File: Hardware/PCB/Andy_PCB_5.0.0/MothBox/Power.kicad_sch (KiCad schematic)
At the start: 27 parts, among them P1 Raw Input, P2 12V Regulated Input, P3 Input to regulator, Q1 BC817, Q2 TJ10S04M3L,LXHQ, U15 Place Holder voltage regulator, U19 INA219BIDCNT, U3 XL4015E1

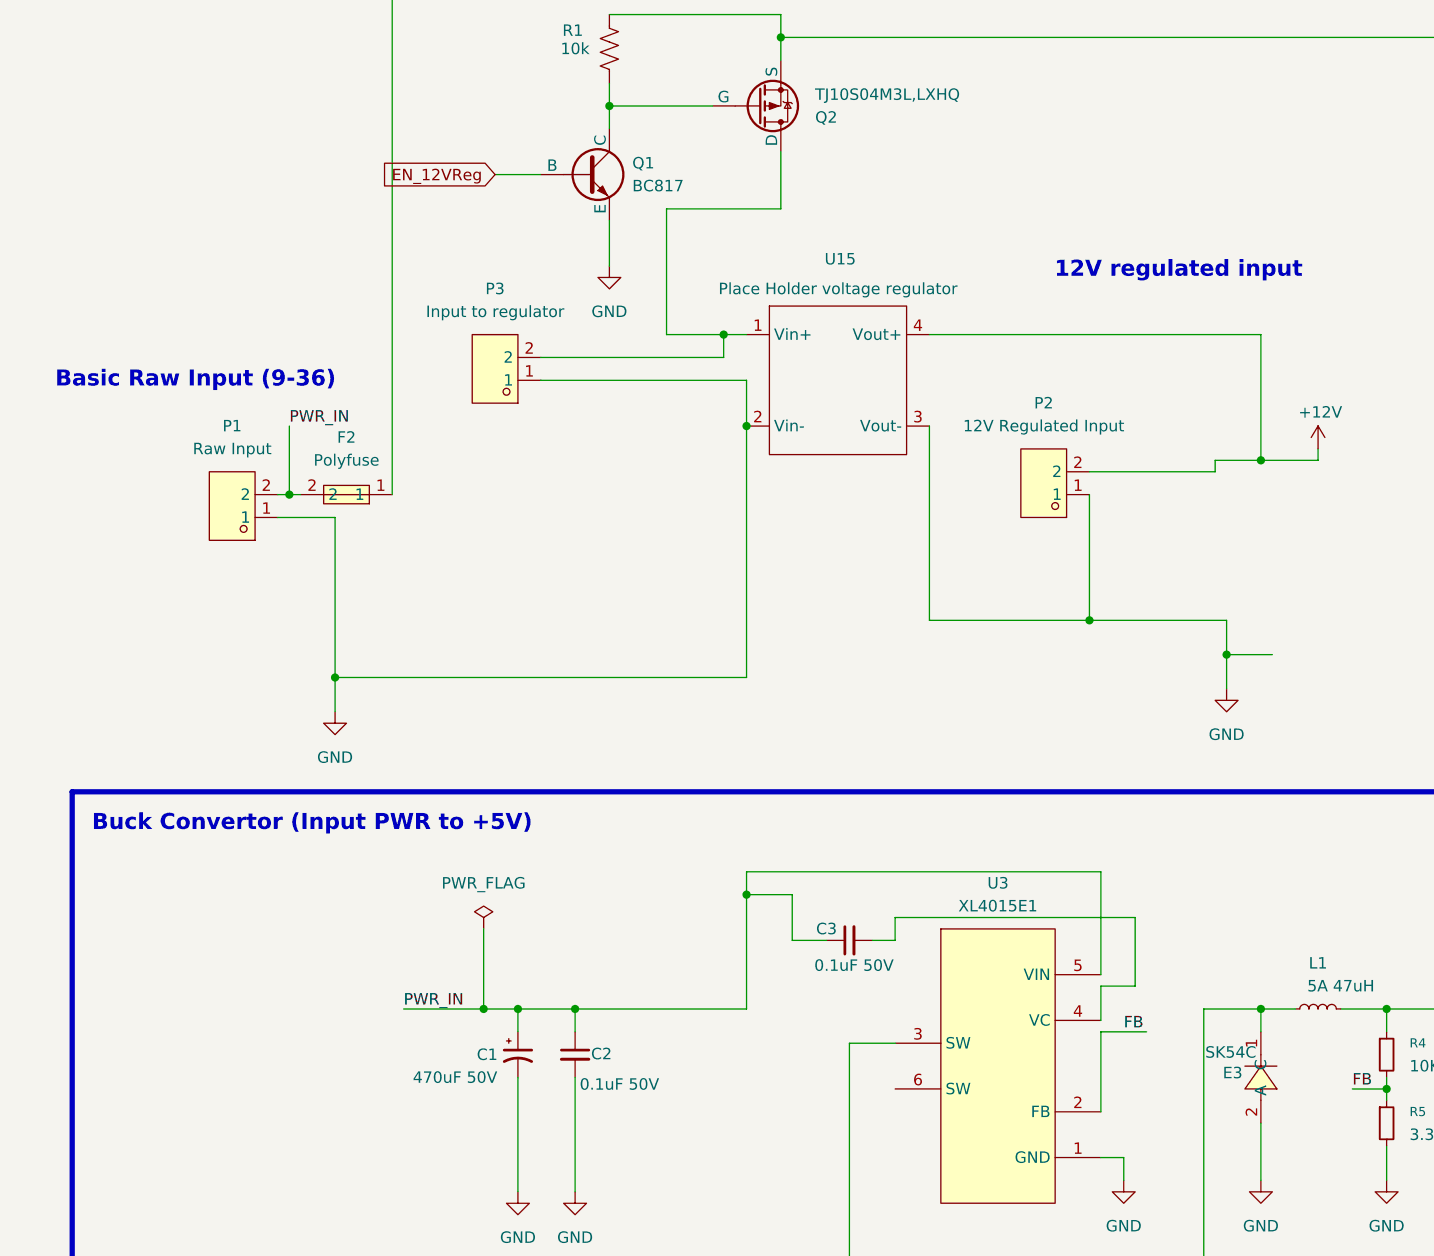
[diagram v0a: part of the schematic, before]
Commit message: cleaned most schematic and got rid of half errors in ERC
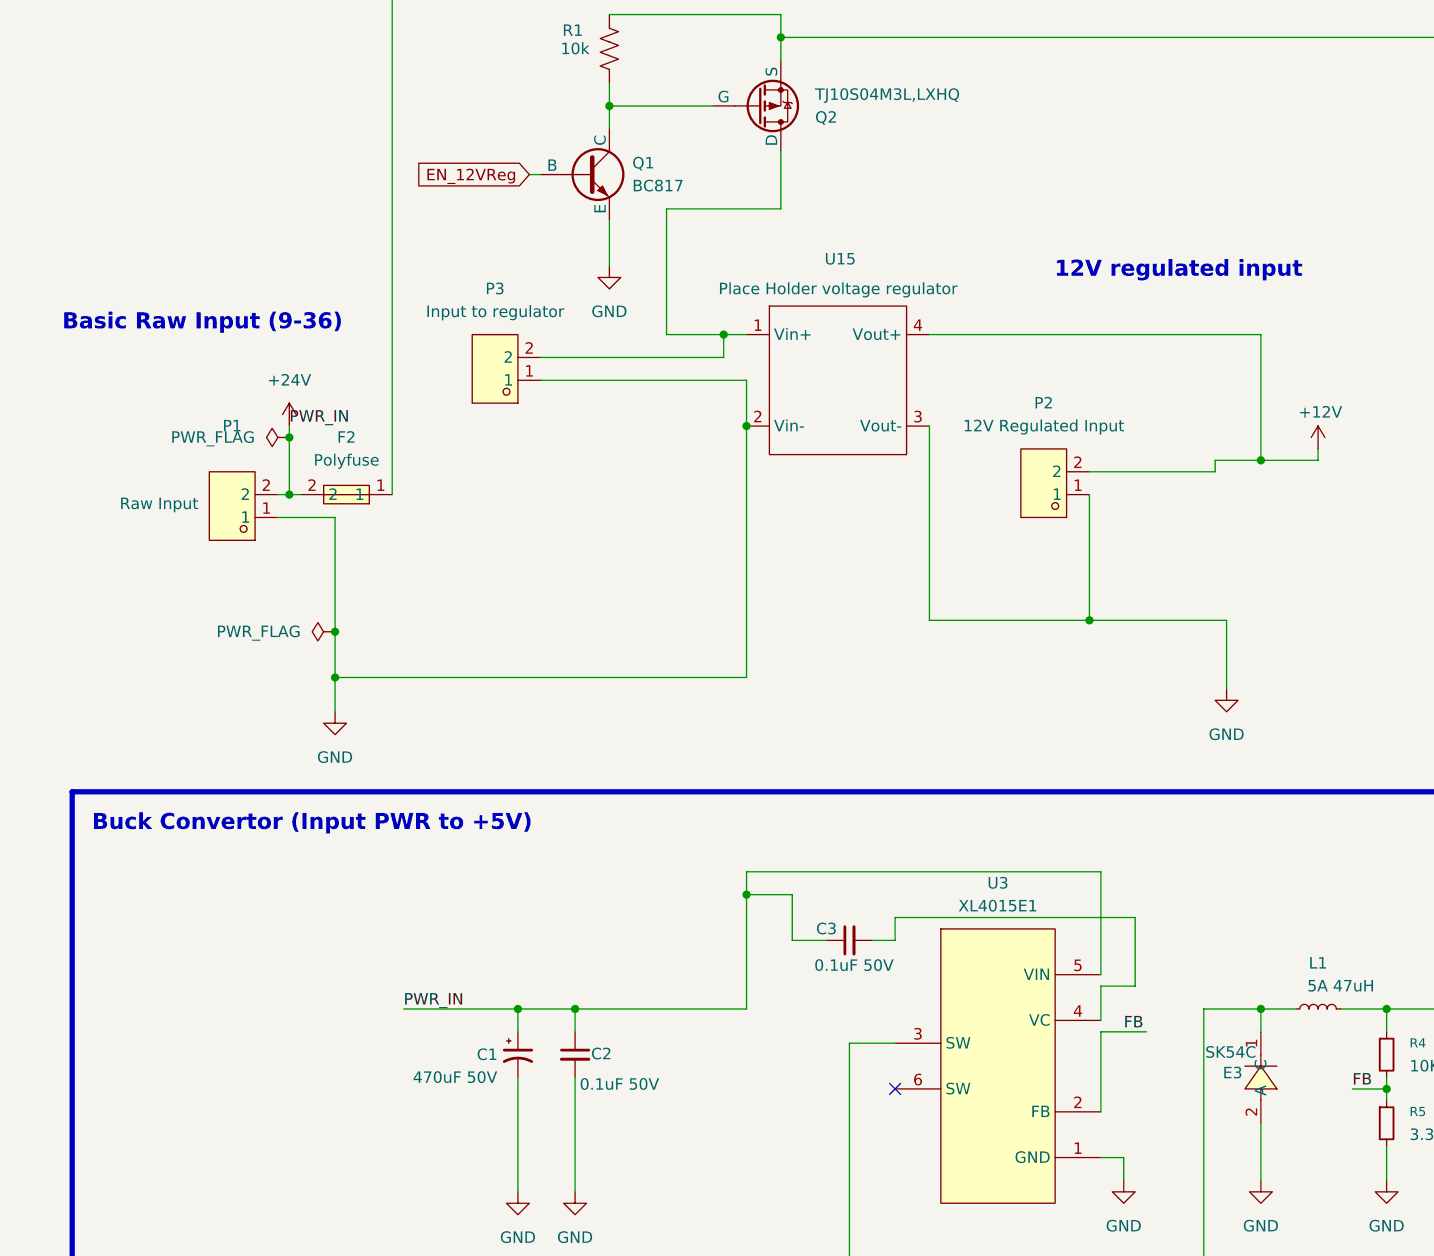
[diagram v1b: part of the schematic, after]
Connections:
- net PWR_IN renamed +24V
- no-connect marks 0 -> 1

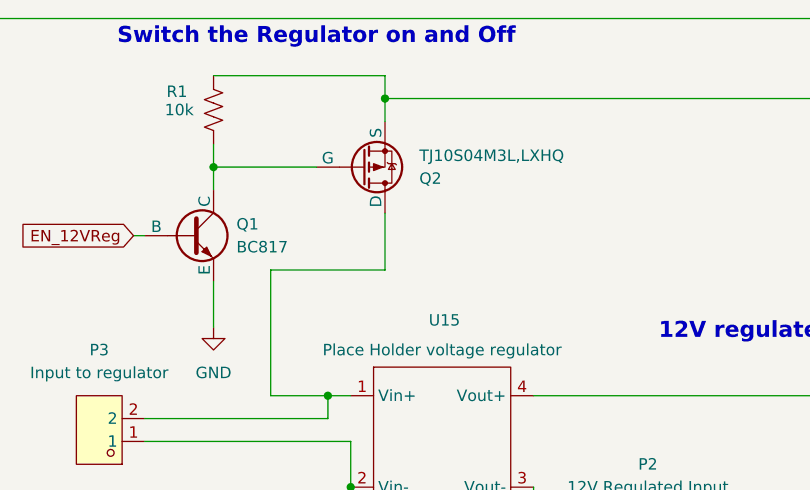
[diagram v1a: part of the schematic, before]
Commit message: Fixed parts with conflicting LCSC footprints
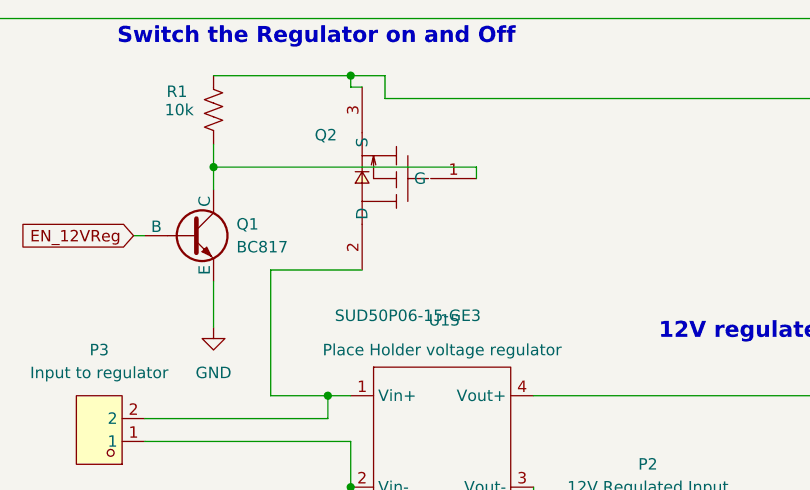
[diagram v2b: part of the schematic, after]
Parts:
- Q2: value TJ10S04M3L,LXHQ -> SUD50P06-15-GE3; footprint Package_TO_SOT_SMD:TO-252-2 -> easyeda2kicad:TO-252-3_L6.5-W5.8-P4.58-BL; symbol Simulation_SPICE:PMOS -> easyeda2kicad:SUD50P06-15-GE3; Digikey Part No TJ10S04M3L,LXHQ -> (none); LCSC Part (none) -> C141584; LCSC Part no  C41355200 -> (none)
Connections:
- net at Q1.3 (C), R1.1: now also Q2.1 (G); no longer Q2.2 (G)
- net at P3.2, U15.1 (Vin+): now also Q2.2 (D); no longer Q2.1 (D)
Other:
- moved on the sheet: Q2
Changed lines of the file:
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@@
 	)
 	(junction
-		(at 106.68 22.86)
+		(at 102.87 20.32)
 		(diameter 0)
 		(color 0 0 0 0)
@@
 	(wire
 		(pts
+			(xy 102.87 20.32) (xy 106.68 20.32)
+		)
+		(stroke
+			(width 0)
+			(type default)
+		)
+	)
+	(wire
+		(pts
 			(xy 267.97 49.53) (xy 267.97 44.45)
 		)
@@
 	(wire
 		(pts
-			(xy 106.68 41.91) (xy 106.68 35.56)
-		)
-		(stroke
-			(width 0)
-			(type default)
-		)
-	)
-	(wire
-		(pts
 			(xy 254 55.88) (xy 257.81 55.88)
 		)
@@
 	(wire
 		(pts
-			(xy 106.68 22.86) (xy 106.68 25.4)
-		)
-		(stroke
-			(width 0)
-			(type default)
-		)
-	)
-	(wire
-		(pts
 			(xy 102.87 118.11) (xy 102.87 130.81)
 		)
@@
 	(wire
 		(pts
-			(xy 93.98 41.91) (xy 106.68 41.91)
+			(xy 93.98 41.91) (xy 104.14 41.91)
 		)
 		(stroke
@@
 	(wire
 		(pts
+			(xy 102.87 21.59) (xy 102.87 20.32)
+		)
+		(stroke
+			(width 0)
+			(type default)
+		)
+	)
+	(wire
+		(pts
 			(xy 100.33 58.42) (xy 100.33 55.88)
 		)
@@
 	(wire
 		(pts
-			(xy 87.63 20.32) (xy 106.68 20.32)
+			(xy 87.63 20.32) (xy 102.87 20.32)
 		)
 		(stroke
@@
 	(wire
 		(pts
+			(xy 104.14 21.59) (xy 102.87 21.59)
+		)
+		(stroke
+			(width 0)
+			(type default)
+		)
+	)
+	(wire
+		(pts
 			(xy 318.77 54.61) (xy 303.53 54.61)
 		)
@@
 	(wire
 		(pts
-			(xy 87.63 30.48) (xy 99.06 30.48)
+			(xy 87.63 30.48) (xy 116.84 30.48)
 		)
 		(stroke
@@
 	(wire
 		(pts
+			(xy 116.84 30.48) (xy 116.84 31.75)
+		)
+		(stroke
+			(width 0)
+			(type default)
+		)
+	)
+	(wire
+		(pts
 			(xy 160.02 143.51) (xy 160.02 149.86)
 		)
@@
 	)
 	(symbol
-		(lib_id "Simulation_SPICE:PMOS")
-		(at 104.14 30.48 0)
-		(mirror x)
+		(lib_id "easyeda2kicad:SUD50P06-15-GE3")
+		(at 109.22 31.75 0)
+		(mirror y)
 		(unit 1)
 		(exclude_from_sim no)
@@
 		(on_board yes)
 		(dnp no)
-		(fields_autoplaced yes)
 		(property "Reference" "Q2"
-			(at 110.49 31.7501 0)
-			(effects
-				(font
-					(size 1.27 1.27)
-				)
-				(justify left)
-			)
-		)
-		(property "Value" "TJ10S04M3L,LXHQ"
-			(at 110.49 29.2101 0)
+			(at 101.346 26.924 0)
 			(effects
 				(font
@@
 			)
 		)
-		(property "Footprint" "Package_TO_SOT_SMD:TO-252-2"
-			(at 109.22 33.02 0)
+		(property "Value" "SUD50P06-15-GE3"
+			(at 109.22 46.99 0)
 			(effects
 				(font
 					(size 1.27 1.27)
 				)
-				(hide yes)
 			)
 		)
-		(property "Datasheet" "https://ngspice.sourceforge.io/docs/ngspice-html-manual/manual.xhtml#cha_MOSFETs"
-			(at 104.14 17.78 0)
+		(property "Footprint" "easyeda2kicad:TO-252-3_L6.5-W5.8-P4.58-BL"
+			(at 109.22 49.53 0)
 			(effects
 				(font
@@
 			)
 		)
-		(property "Description" "P-Channel 40 V 10A (Ta) 27W (Tc) Surface Mount DPAK+"
-			(at 104.14 30.48 0)
+		(property "Datasheet" "https://lcsc.com/product-detail/MOSFET_VISHAY_SUD50P06-15-GE3_SUD50P06-15-GE3_C141584.html"
+			(at 109.22 52.07 0)
 			(effects
 				(font
@@
 			)
 		)
-		(property "Sim.Device" "PMOS"
-			(at 104.14 13.335 0)
-			(effects
-				(font
-					(size 1.27 1.27)
-				)
-				(hide yes)
-			)
-		)
-		(property "Sim.Type" "VDMOS"
-			(at 104.14 11.43 0)
-			(effects
-				(font
-					(size 1.27 1.27)
-				)
-				(hide yes)
-			)
-		)
-		(property "Sim.Pins" "1=D 2=G 3=S"
-			(at 104.14 15.24 0)
-			(effects
-				(font
-					(size 1.27 1.27)
-				)
-				(hide yes)
-			)
-		)
-		(property "LCSC Part no " "C41355200"
-			(at 104.14 30.48 0)
+		(property "Description" ""
+			(at 109.22 31.75 0)
 			(effects
 				(font
@@
 			)
 		)
-		(property "Digikey Part No" "TJ10S04M3L,LXHQ"
-			(at 104.14 30.48 0)
+		(property "LCSC Part" "C141584"
+			(at 109.22 54.61 0)
 			(effects
 				(font
@@
 			)
 		)
-		(property "LCSC PN" ""
-			(at 104.14 30.48 0)
-			(effects
-				(font
-					(size 1.27 1.27)
-				)
-			)
-		)

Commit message: Maybe these files needed saving too for paul?
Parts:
- C1, C4: symbol Device:C_Polarized_Small_US -> MB_Library:C_Polarized_Small_US
- C2, C3, C5: symbol Device:C_Small -> MB_Library:C_Small
- C6: symbol easyeda2kicad:CC0603KRX7R9BB104 -> MB_Library:CC0603KRX7R9BB104
- E3: symbol easyeda2kicad:SK54C_C5449119 -> MB_Library:SK54C_C5449119
- F2: symbol easyeda2kicad:0805L010_60WR -> MB_Library:0805L010_60WR
- L1: symbol Device:L_Small -> MB_Library:L_Small
- P1, P2, P3: symbol easyeda2kicad:DB142R-5.08-2P -> MB_Library:DB142R-5.08-2P
- Q1: symbol BC817:BC817_NPN_BJT -> MB_Library:BC817_NPN_BJT
- Q2: symbol easyeda2kicad:SUD50P06-15-GE3 -> MB_Library:SUD50P06-15-GE3
- R1: symbol Device:R_US -> MB_Library:R_US
- R4, R5: symbol Device:R_Small -> MB_Library:R_Small
- R63: symbol easyeda2kicad:PCSR2512BR100M6 -> MB_Library:PCSR2512BR100M6
- R64, R65: symbol easyeda2kicad:FRC0603J103TS -> MB_Library:FRC0603J103TS
- TP1, TP2, TP3, TP4: symbol Connector:TestPoint -> MB_Library:TestPoint
- U15: symbol New_Library:Buck-Boost -> MB_Library:Buck-Boost
- U19: symbol easyeda2kicad:INA219AIDCNR -> MB_Library:INA219AIDCNR
- U3: symbol easyeda2kicad:XL4015E1 -> MB_Library:XL4015E1
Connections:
- net GND: no longer C6.1, U19.3 (GND)
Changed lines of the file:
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@@
 	)
 	(symbol
-		(lib_id "power:GND")
+		(lib_id "MB_Library:GND")
 		(at 156.21 95.25 0)
 		(unit 1)
@@
 	)
 	(symbol
-		(lib_id "BC817:BC817_NPN_BJT")
+		(lib_id "MB_Library:BC817_NPN_BJT")
 		(at 85.09 38.1 0)
 		(unit 1)
@@
 	)
 	(symbol
-		(lib_id "easyeda2kicad:PCSR2512BR100M6")
+		(lib_id "MB_Library:PCSR2512BR100M6")
 		(at 273.05 52.07 90)
 		(unit 1)
@@
 	)
 	(symbol
-		(lib_id "easyeda2kicad:DB142R-5.08-2P")
+		(lib_id "MB_Library:DB142R-5.08-2P")
 		(at 135.89 72.39 180)
 		(unit 1)
@@
 	)
 	(symbol
-		(lib_id "easyeda2kicad:DB142R-5.08-2P")
+		(lib_id "MB_Library:DB142R-5.08-2P")
 		(at 74.93 59.69 180)
 		(unit 1)
@@
 	)
 	(symbol
-		(lib_id "easyeda2kicad:SK54C_C5449119")
+		(lib_id "MB_Library:SK54C_C5449119")
 		(at 160.02 138.43 270)
 		(unit 1)
@@
 	)
 	(symbol
-		(lib_id "easyeda2kicad:XL4015E1")
+		(lib_id "MB_Library:XL4015E1")
 		(at 130.81 137.16 0)
 		(unit 1)
@@
 	)
 	(symbol
-		(lib_id "Connector:TestPoint")
+		(lib_id "MB_Library:TestPoint")
 		(at 269.24 62.23 180)
 		(unit 1)
@@
 	)
 	(symbol
-		(lib_id "power:+12V")
+		(lib_id "MB_Library:+12V")
 		(at 166.37 68.58 0)
 		(unit 1)
@@
 	)
 	(symbol
-		(lib_id "power:+24V")
+		(lib_id "MB_Library:+24V")
 		(at 52.07 66.04 0)
 		(unit 1)
@@
 	)
 	(symbol
-		(lib_id "power:PWR_FLAG")
+		(lib_id "MB_Library:PWR_FLAG")
 		(at 52.07 67.31 90)
 		(unit 1)
@@
 	)
 	(symbol
-		(lib_id "easyeda2kicad:CC0603KRX7R9BB104")
+		(lib_id "MB_Library:CC0603KRX7R9BB104")
 		(at 214.63 41.91 90)
 		(unit 1)
@@
 	)
 	(symbol
-		(lib_id "Connector:TestPoint")
+		(lib_id "MB_Library:TestPoint")
 		(at 232.41 57.15 90)
 		(unit 1)
@@
 	)
 	(symbol
-		(lib_id "Connector:TestPoint")
+		(lib_id "MB_Library:TestPoint")
 		(at 223.52 54.61 90)
 		(unit 1)
@@
 	)
 	(symbol
-		(lib_id "power:GND")
+		(lib_id "MB_Library:GND")
 		(at 200.66 149.86 0)
 		(unit 1)
@@
 	)
 	(symbol
-		(lib_id "Device:C_Small")
+		(lib_id "MB_Library:C_Small")
 		(at 200.66 138.43 0)
 		(unit 1)
@@
 	)
 	(symbol
-		(lib_id "Adafruit_INA219_CurPowerMonitor-eagle-import:GND")
+		(lib_id "MB_Library:GND")
 		(at 229.87 74.93 0)
 		(unit 1)
@@
 	)
 	(symbol
-		(lib_id "Device:L_Small")
+		(lib_id "MB_Library:L_Small")
 		(at 166.37 130.81 90)
 		(unit 1)
@@
 	)
 	(symbol
-		(lib_id "power:+3.3V")
+		(lib_id "MB_Library:+3.3V")
 		(at 295.91 31.75 0)
 		(unit 1)
@@
 	)
 	(symbol
-		(lib_id "Device:C_Small")
+		(lib_id "MB_Library:C_Small")
 		(at 114.3 123.19 90)
 		(unit 1)
@@
 	)
 	(symbol
-		(lib_id "power:GND")
+		(lib_id "MB_Library:GND")
 		(at 83.82 151.13 0)
 		(unit 1)
@@
 	)
 	(symbol
-		(lib_id "power:PWR_FLAG")
+		(lib_id "MB_Library:PWR_FLAG")
 		(at 57.15 88.9 90)
 		(unit 1)
@@
 	)
 	(symbol
-		(lib_id "power:GND")
+		(lib_id "MB_Library:GND")
 		(at 187.96 149.86 0)
 		(unit 1)
@@
 	)
 	(symbol
-		(lib_id "Device:R_Small")
+		(lib_id "MB_Library:R_Small")
 		(at 173.99 143.51 0)
 		(unit 1)
@@
 	)
 	(symbol
-		(lib_id "easyeda2kicad:DB142R-5.08-2P")
+		(lib_id "MB_Library:DB142R-5.08-2P")
 		(at 45.72 74.93 180)
 		(unit 1)
@@
 	)
 	(symbol
-		(lib_id "power:GND")
+		(lib_id "MB_Library:GND")
 		(at 77.47 151.13 0)
 		(unit 1)
@@
 	)
 	(symbol
-		(lib_id "power:GND")
+		(lib_id "MB_Library:GND")
 		(at 144.78 149.86 0)
 		(unit 1)
@@
 	)
 	(symbol
-		(lib_id "Connector:TestPoint")
+		(lib_id "MB_Library:TestPoint")
 		(at 190.5 130.81 0)
 		(unit 1)
@@
 	)
 	(symbol
-		(lib_id "Device:R_Small")
+		(lib_id "MB_Library:R_Small")
 		(at 173.99 135.89 0)
 		(unit 1)
@@
 	)
 	(symbol
-		(lib_id "Adafruit_INA219_CurPowerMonitor-eagle-import:GND")
+		(lib_id "MB_Library:GND")
 		(at 207.01 49.53 0)
 		(unit 1)
@@
 	)
 	(symbol
-		(lib_id "easyeda2kicad:FRC0603J103TS")
+		(lib_id "MB_Library:FRC0603J103TS")
 		(at 295.91 39.37 90)
 		(unit 1)
@@
 	)
 	(symbol
-		(lib_id "Device:C_Polarized_Small_US")
+		(lib_id "MB_Library:C_Polarized_Small_US")
 		(at 77.47 135.89 0)
 		(unit 1)
@@
 	)
 	(symbol
-		(lib_id "Device:R_US")
+		(lib_id "MB_Library:R_US")
 		(at 87.63 24.13 180)
 		(unit 1)
@@
 	)
 	(symbol
-		(lib_id "New_Library:Buck-Boost")
+		(lib_id "MB_Library:Buck-Boost")
 		(at 113.03 60.96 0)
 		(unit 1)
@@
 	)
 	(symbol
-		(lib_id "power:GND")
+		(lib_id "MB_Library:GND")
 		(at 173.99 149.86 0)
 		(unit 1)
@@
 	)
 	(symbol
-		(lib_id "power:GND")
+		(lib_id "MB_Library:GND")
 		(at 57.15 97.79 0)
 		(unit 1)
@@
 	)
 	(symbol
-		(lib_id "power:+5V")
+		(lib_id "MB_Library:+5V")
 		(at 200.66 129.54 0)
 		(unit 1)
@@
 	)
 	(symbol
-		(lib_id "power:GND")
+		(lib_id "MB_Library:GND")
 		(at 160.02 149.86 0)
 		(unit 1)
@@
 	)
 	(symbol
-		(lib_id "easyeda2kicad:INA219AIDCNR")
+		(lib_id "MB_Library:INA219AIDCNR")
 		(at 243.84 52.07 180)
 		(unit 1)
@@
 	)
 	(symbol
-		(lib_id "easyeda2kicad:SUD50P06-15-GE3")
+		(lib_id "MB_Library:SUD50P06-15-GE3")
 		(at 109.22 31.75 0)
 		(mirror y)
@@
 	)
 	(symbol
-		(lib_id "power:+3.3V")
+		(lib_id "MB_Library:+3.3V")
 		(at 207.01 31.75 0)
 		(unit 1)
@@
 	)
 	(symbol
-		(lib_id "easyeda2kicad:FRC0603J103TS")
+		(lib_id "MB_Library:FRC0603J103TS")
 		(at 303.53 39.37 90)
 		(unit 1)
@@
 	)
 	(symbol
-		(lib_id "Device:C_Polarized_Small_US")
+		(lib_id "MB_Library:C_Polarized_Small_US")
 		(at 187.96 138.43 0)
 		(unit 1)
@@
 	)
 	(symbol
-		(lib_id "Device:C_Small")
+		(lib_id "MB_Library:C_Small")
 		(at 83.82 135.89 0)
 		(unit 1)
@@
 	)
 	(symbol
-		(lib_id "easyeda2kicad:0805L010_60WR")
+		(lib_id "MB_Library:0805L010_60WR")
 		(at 58.42 73.66 180)
 		(unit 1)
@@
 	)
 	(symbol
-		(lib_id "power:GND")
+		(lib_id "MB_Library:GND")
 		(at 87.63 48.26 0)
 		(unit 1)
@@
 	)
 	(symbol
-		(lib_id "power:+3.3V")
+		(lib_id "MB_Library:+3.3V")
 		(at 303.53 31.75 0)
 		(unit 1)
